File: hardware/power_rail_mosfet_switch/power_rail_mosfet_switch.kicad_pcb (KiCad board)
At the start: 2 copper layers, 40 x 12 mm, 8 parts, among them J1 Screw_Terminal_01x03, J2 Screw_Terminal_01x02, Q1 HXY2102EI, Q2 AO3401A

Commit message: text layput for back silkscreen next to connectors
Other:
- outline, holes or cut-outs redrawn
- board text added: "CTRL"
- board text added: "GND"
- board text added: "Power Switch V1.0"
- board text added: "Sep 2026"
- board text added: "VIN"
- board text added: "VOUT"

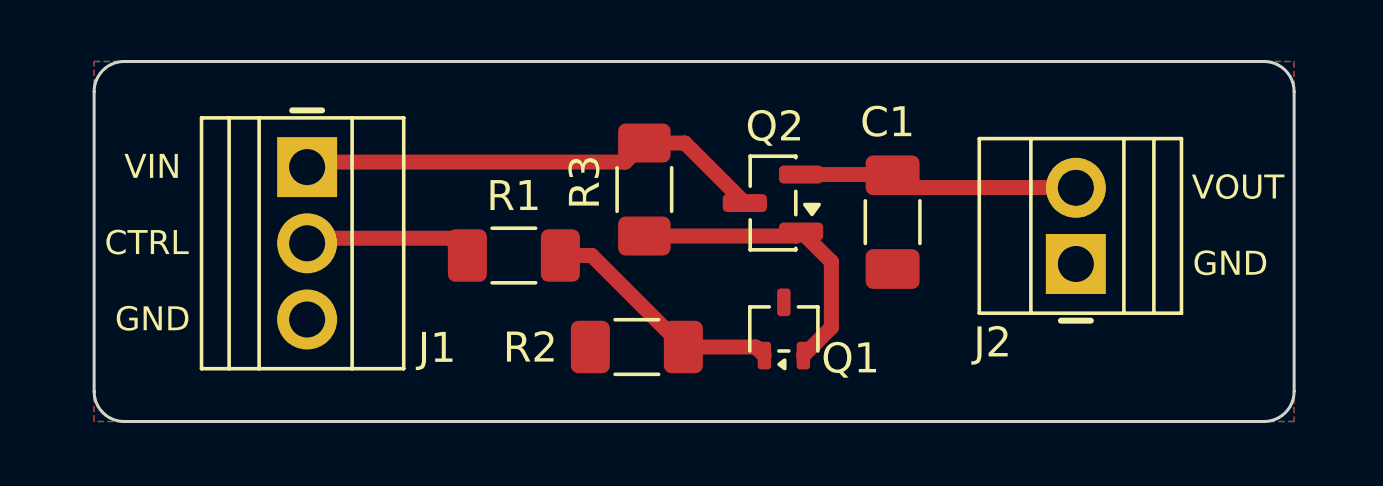
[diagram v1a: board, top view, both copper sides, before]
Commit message: cleanup scripts, particulariy centering
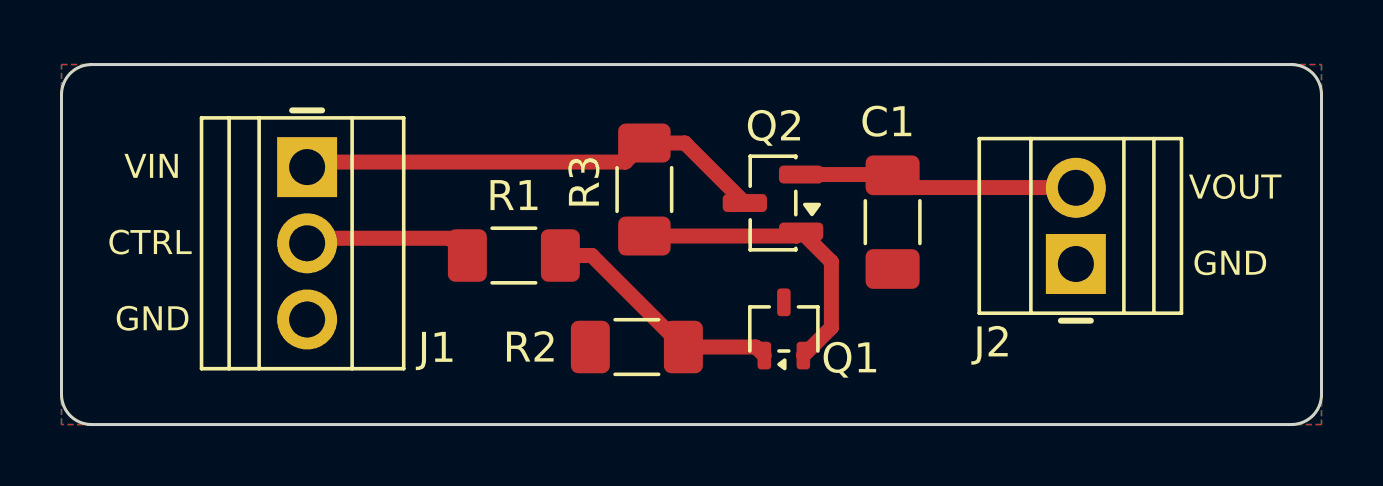
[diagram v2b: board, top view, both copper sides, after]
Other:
- board size 40 x 12 mm -> 42 x 12 mm
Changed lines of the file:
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@@
 	)
 	(gr_arc
-		(start 120 51)
-		(mid 120.292893 50.292893)
-		(end 121 50)
+		(start 118.912491 51.101244)
+		(mid 119.205385 50.394137)
+		(end 119.912491 50.101244)
 		(stroke
 			(width 0.1)
@@
 	)
 	(gr_line
-		(start 120 61)
-		(end 120 51)
+		(start 118.912491 61.101244)
+		(end 118.912491 51.101244)
 		(stroke
 			(width 0.1)
@@
 	)
 	(gr_line
-		(start 121 50)
-		(end 159 50)
+		(start 119.912491 50.101244)
+		(end 159.912492 50.101244)
 		(stroke
 			(width 0.1)
@@
 	)
 	(gr_arc
-		(start 121 62)
-		(mid 120.292893 61.707106)
-		(end 120 61)
+		(start 119.912491 62.101244)
+		(mid 119.205385 61.80835)
+		(end 118.912491 61.101244)
 		(stroke
 			(width 0.1)
@@
 	)
 	(gr_arc
-		(start 159 50)
-		(mid 159.707106 50.292893)
-		(end 160 51)
+		(start 159.912492 50.101244)
+		(mid 160.619598 50.394137)
+		(end 160.912492 51.101244)
 		(stroke
 			(width 0.1)
@@
 	)
 	(gr_line
-		(start 159 62)
-		(end 121 62)
+		(start 159.912492 62.101244)
+		(end 119.912491 62.101244)
 		(stroke
 			(width 0.1)
@@
 	)
 	(gr_line
-		(start 160 51)
-		(end 160 61)
+		(start 160.912492 51.101244)
+		(end 160.912492 61.101244)
 		(stroke
 			(width 0.1)
@@
 	)
 	(gr_arc
-		(start 160 61)
-		(mid 159.707106 61.707106)
-		(end 159 62)
+		(start 160.912492 61.101244)
+		(mid 160.619598 61.80835)
+		(end 159.912492 62.101244)
 		(stroke
 			(width 0.1)
@@
 	)
 	(gr_text "CTRL"
-		(at 121.751429 56.5165 0)
+		(at 121.851429 56.5165 0)
 		(layer "F.SilkS")
 		(effects
@@
 	)
 	(gr_text "VOUT"
-		(at 158.130714 54.6665 0)
+		(at 158.030714 54.6665 0)
 		(layer "F.SilkS")
 		(effects
@@
 	)
 	(gr_text "CTRL"
-		(at 120.252858 55.6035 180)
+		(at 121.602858 55.6035 180)
 		(layer "B.SilkS")
 		(effects
@@
 	)
 	(gr_text "GND"
-		(at 120.660953 58.1435 180)
+		(at 122.021906 58.1435 180)
 		(layer "B.SilkS")
 		(effects
@@
 	)
 	(gr_text "VIN"
-		(at 120.92762 53.0635 180)
+		(at 122.55524 53.0635 180)
 		(layer "B.SilkS")
 		(effects
@@
 	)
 	(gr_text "VOUT"
-		(at 156.575 53.7535 180)
+		(at 155.225 53.7535 180)
 		(layer "B.SilkS")
 		(effects
@@
 	)
 	(gr_text "GND"
-		(at 156.585953 56.2935 180)
+		(at 155.225 56.2935 180)
 		(layer "B.SilkS")
 		(effects
@@
 		(polygon
 			(pts
-				(xy 120 50) (xy 160 50) (xy 160 62) (xy 120 62)
+				(xy 118.912491 50.101244) (xy 160.912492 50.101244) (xy 160.912492 62.101244) (xy 118.912491 62.101244)
 			)
 		)
@@
 		(polygon
 			(pts
-				(xy 120 50) (xy 160 50) (xy 160 62) (xy 120 62)
-			)
-		)
+				(xy 118.912491 50.101244) (xy 160.912492 50.101244) (xy 160.912492 62.101244) (xy 118.912491 62.101244)
+			)
+		)
